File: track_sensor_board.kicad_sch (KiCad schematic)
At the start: 27 parts, among them J1 Barrel_Jack, J10 Screw_Terminal_01x02, J11 Screw_Terminal_01x02, J2 10-18-1032, J3 10-18-1032, J4 10-18-1032, J5 10-18-1032, J6 10-18-1032, J7 10-18-1032, J8 10-18-1032, J9 10-18-1032, SW1 SW_DIP_x04, U1 MCP23017_SP, U2 TSR_1-2450

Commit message: chore: save after recovery, looks good
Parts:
- A1: footprint Module:Adafruit_Ethernet_Featherwing -> Adafruit:Adafruit_Ethernet_Featherwing
- J2, J3, J4, J5, J6, J7, J8, J9: footprint Connector_Molex:CONN_10-18-1032_MOL -> Conn_Molex:CONN_10-18-1032_MOL
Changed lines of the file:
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@@
       (effects (font (size 1.524 1.524)) (justify left))
     )
-    (property "Footprint" "Connector_Molex:CONN_10-18-1032_MOL" (at 518.16 269.24 0)
+    (property "Footprint" "Conn_Molex:CONN_10-18-1032_MOL" (at 518.16 269.24 0)
       (effects (font (size 1.27 1.27) italic) hide)
     )
@@
       (effects (font (size 1.524 1.524)) (justify left))
     )
-    (property "Footprint" "Connector_Molex:CONN_10-18-1032_MOL" (at 518.16 180.34 0)
+    (property "Footprint" "Conn_Molex:CONN_10-18-1032_MOL" (at 518.16 180.34 0)
       (effects (font (size 1.27 1.27) italic) hide)
     )
@@
       (effects (font (size 1.524 1.524)) (justify left))
     )
-    (property "Footprint" "Connector_Molex:CONN_10-18-1032_MOL" (at 518.16 193.04 0)
+    (property "Footprint" "Conn_Molex:CONN_10-18-1032_MOL" (at 518.16 193.04 0)
       (effects (font (size 1.27 1.27) italic) hide)
     )
@@
       (effects (font (size 1.524 1.524)) (justify left))
     )
-    (property "Footprint" "Connector_Molex:CONN_10-18-1032_MOL" (at 518.16 218.44 0)
+    (property "Footprint" "Conn_Molex:CONN_10-18-1032_MOL" (at 518.16 218.44 0)
       (effects (font (size 1.27 1.27) italic) hide)
     )
@@
       (effects (font (size 1.524 1.524)) (justify left))
     )
-    (property "Footprint" "Connector_Molex:CONN_10-18-1032_MOL" (at 518.16 243.84 0)
+    (property "Footprint" "Conn_Molex:CONN_10-18-1032_MOL" (at 518.16 243.84 0)
       (effects (font (size 1.27 1.27) italic) hide)
     )
@@
       (effects (font (size 1.524 1.524)) (justify left))
     )
-    (property "Footprint" "Connector_Molex:CONN_10-18-1032_MOL" (at 518.16 205.74 0)
+    (property "Footprint" "Conn_Molex:CONN_10-18-1032_MOL" (at 518.16 205.74 0)
       (effects (font (size 1.27 1.27) italic) hide)
     )
@@
       (effects (font (size 1.524 1.524)) (justify left))
     )
-    (property "Footprint" "Connector_Molex:CONN_10-18-1032_MOL" (at 518.16 231.14 0)
+    (property "Footprint" "Conn_Molex:CONN_10-18-1032_MOL" (at 518.16 231.14 0)
       (effects (font (size 1.27 1.27) italic) hide)
     )
@@
       (effects (font (size 1.524 1.524)) (justify left))
     )
-    (property "Footprint" "Connector_Molex:CONN_10-18-1032_MOL" (at 518.16 256.54 0)
+    (property "Footprint" "Conn_Molex:CONN_10-18-1032_MOL" (at 518.16 256.54 0)
       (effects (font (size 1.27 1.27) italic) hide)
     )
@@
       (effects (font (size 1.27 1.27)) (justify left))
     )
-    (property "Footprint" "Module:Adafruit_Ethernet_Featherwing" (at 259.08 222.25 0)
+    (property "Footprint" "Adafruit:Adafruit_Ethernet_Featherwing" (at 259.08 222.25 0)
       (effects (font (size 1.27 1.27)) (justify left) hide)
     )

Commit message: feat: mostly updated v1.1
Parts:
- removed JP1: SolderJumper_3_Bridged12, Jumper:SolderJumper-3_P1.3mm_Bridged2Bar12_RoundedPad1.0x1.5mm, symbol Jumper:SolderJumper_3_Bridged12
- added F1: Fuse, Fuse:Fuseholder_Blade_Mini_Keystone_3568, symbol Device:Fuse
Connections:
- net +12V: now also F1.2; no longer J1.1
- net +5V: now also RN1.1 (common), RN2.1 (common)
- net at U1.19 (INTB): now also A3.19 (D5)
- net at U1.20 (INTA): now also A3.20 (D6)
- new net: F1.1, J1.1
- no-connect marks 0 -> 12
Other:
- moved on the sheet: A1, A3, C1, H1, H2, H3, H4, J1, J10, J11, J2, J3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

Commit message: feat: cleaned up a bit
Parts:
- A1: symbol MCU_Module:Adafruit_Ethernet_Featherwing -> Adafruit:Adafruit_Ethernet_Featherwing
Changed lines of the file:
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@@
     )
   )
-  (symbol (lib_id "MCU_Module:Adafruit_Ethernet_Featherwing") (at 198.12 171.45 0) (mirror y) (unit 1)
+  (symbol (lib_id "Adafruit:Adafruit_Ethernet_Featherwing") (at 198.12 171.45 0) (mirror y) (unit 1)
     (in_bom yes) (on_board yes) (dnp no)
     (property "Reference" "A1" (at 186.69 187.96 0)

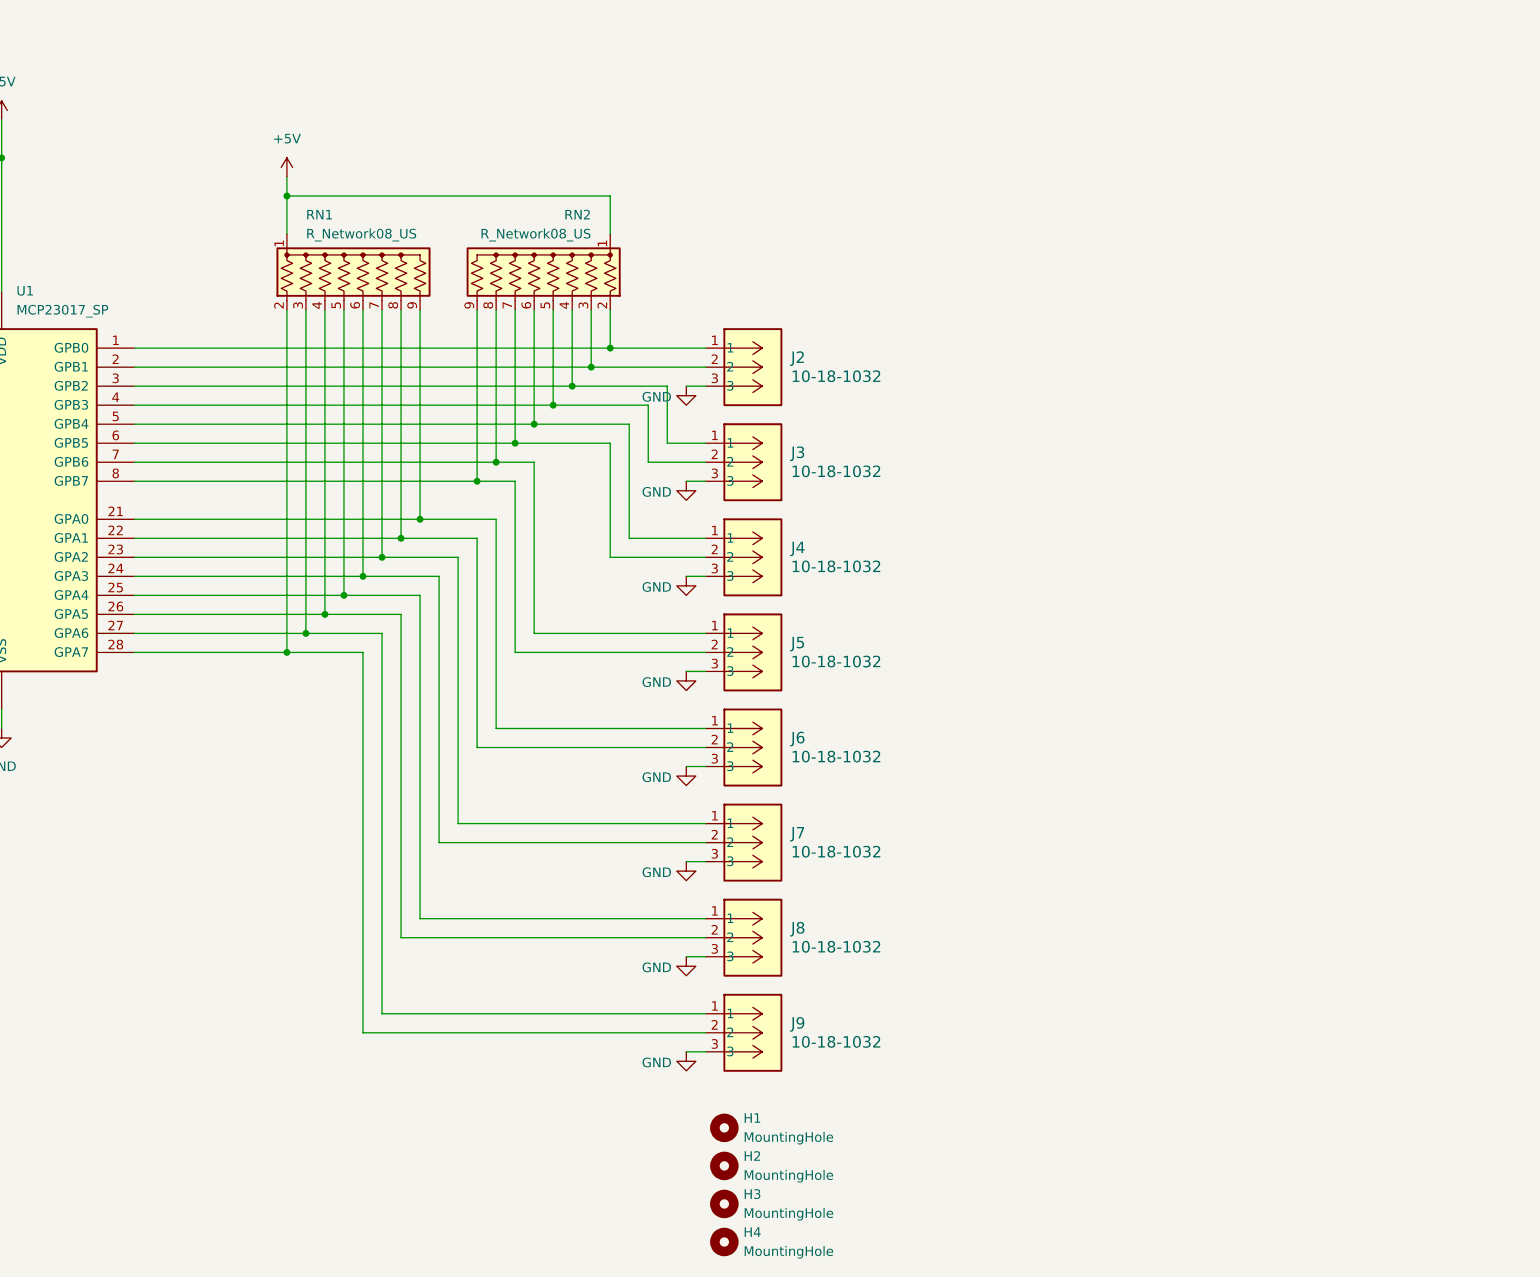
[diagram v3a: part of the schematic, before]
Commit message: feat: added filter caps
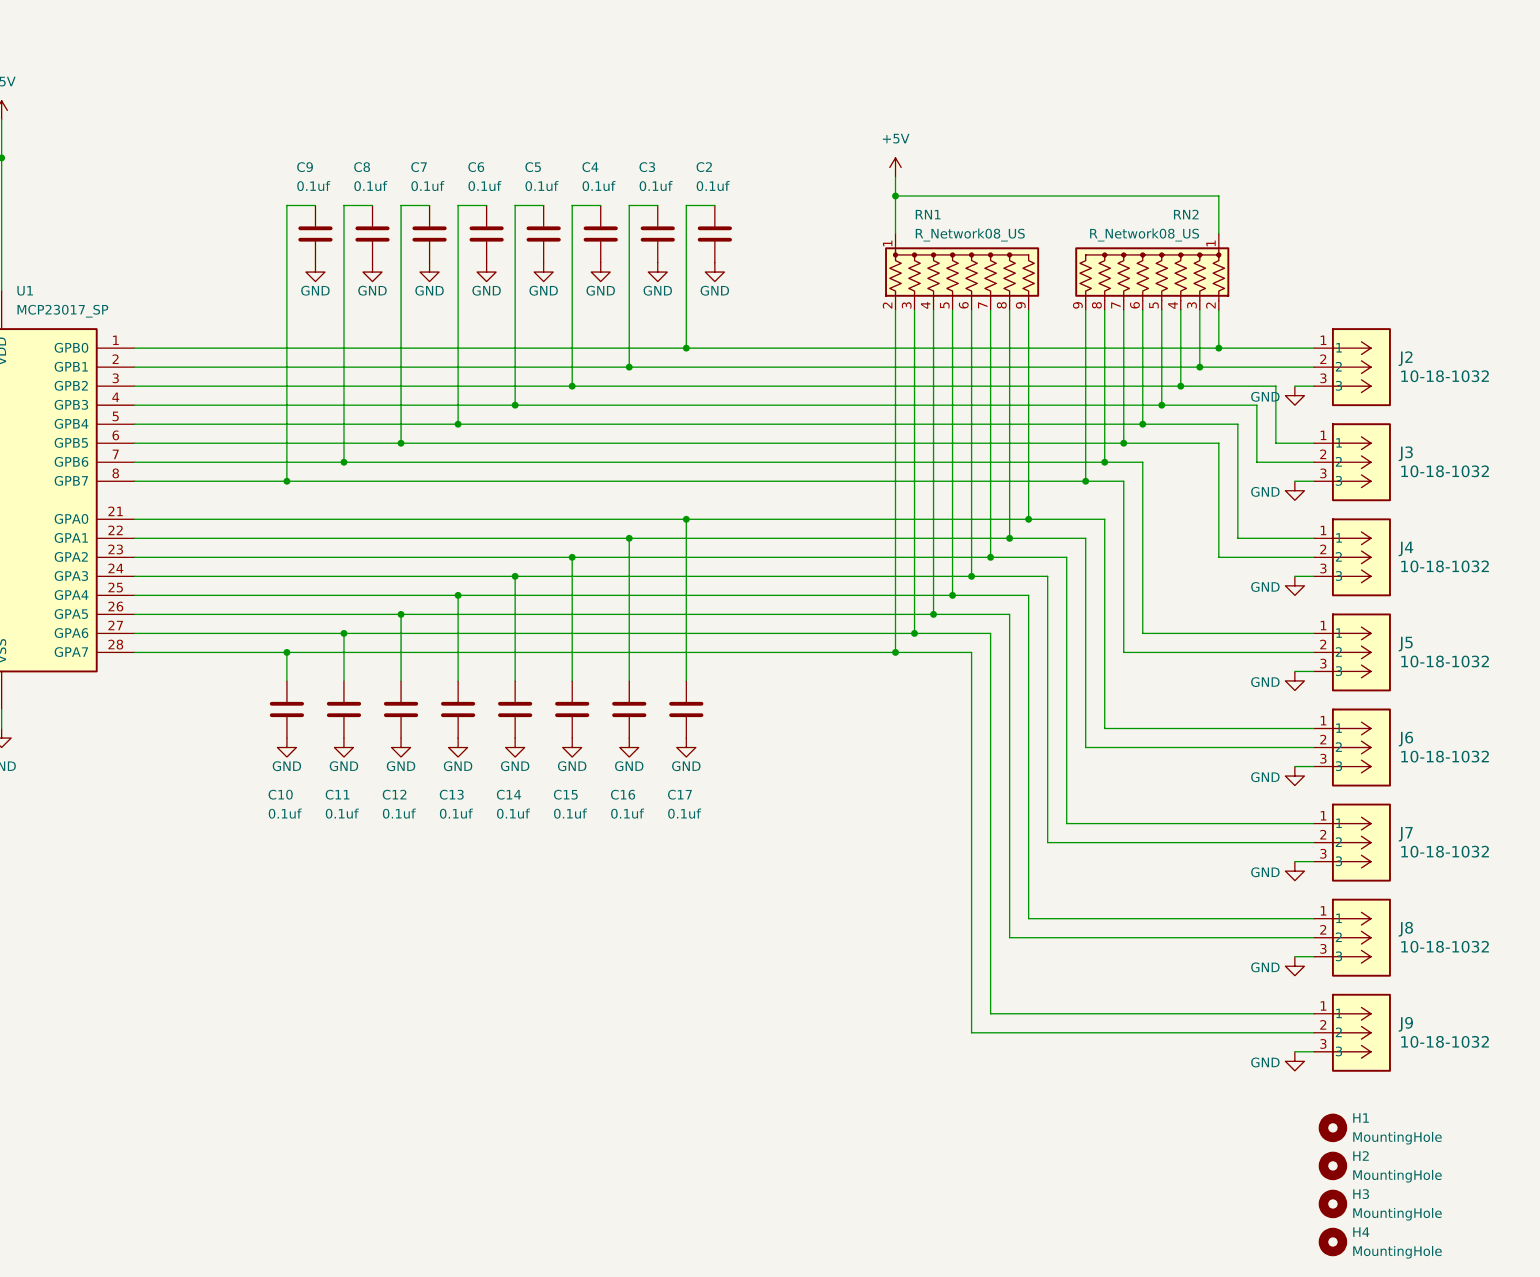
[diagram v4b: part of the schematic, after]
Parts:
- added C10, C11, C12, C13, C14, C15, C16, C17, C2, C3, C4, C5, C6, C7, C8, C9: 0.1uf, Capacitor_THT:C_Disc_D3.0mm_W1.6mm_P2.50mm, symbol Device:C
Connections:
- net GND: now also C10.2, C11.2, C12.2, C13.2, C14.2, C15.2, C16.2, C17.2, C2.2, C3.2, C4.2, C5.2, C6.2, C7.2, C8.2, C9.2
- net at J9.1, RN1.3 (R2), U1.27 (GPA6): now also C11.1
- net at J9.2, RN1.2 (R1), U1.28 (GPA7): now also C10.1
- net at J2.1, RN2.2 (R1), U1.1 (GPB0): now also C2.1
- net at J2.2, RN2.3 (R2), U1.2 (GPB1): now also C3.1
- net at J3.1, RN2.4 (R3), U1.3 (GPB2): now also C4.1
- net at J3.2, RN2.5 (R4), U1.4 (GPB3): now also C5.1
- net at J5.1, RN2.8 (R7), U1.7 (GPB6): now also C8.1
- net at J5.2, RN2.9 (R8), U1.8 (GPB7): now also C9.1
- net at J7.1, RN1.7 (R6), U1.23 (GPA2): now also C15.1
- net at J7.2, RN1.6 (R5), U1.24 (GPA3): now also C14.1
- net at J4.1, RN2.6 (R5), U1.5 (GPB4): now also C6.1
- net at J4.2, RN2.7 (R6), U1.6 (GPB5): now also C7.1
- net at J6.1, RN1.9 (R8), U1.21 (GPA0): now also C17.1
- net at J6.2, RN1.8 (R7), U1.22 (GPA1): now also C16.1
- net at J8.1, RN1.5 (R4), U1.25 (GPA4): now also C13.1
- net at J8.2, RN1.4 (R3), U1.26 (GPA5): now also C12.1
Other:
- moved on the sheet: H1, H2, H3, H4, J2, J3, J4, J5, J6, J7, J8, J9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
